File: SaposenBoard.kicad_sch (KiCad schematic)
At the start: 66 parts, among them IC1 BSO220, IC2 BSO220, IC3 BSO220, IC4 BSO220, J1 ADC4ch, J2 Extra2ch+LED, J3 Encoder1, J4 Encoder2, J5 I2C, J6 Battery, J7 Motor1, J8 Motor2, Q2 IRLML6344, SW1 BatterySW, SW2 SW_Push, SW3 SW_Push, U1 A4955GLPTR-T, U2 A4955GLPTR-T, U3 MPU-6500, U4 NUCLEO-F303K8

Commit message: [add]配線できた
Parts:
- removed J4: Encoder2, Connector_Molex:Molex_Micro-Latch_53253-0470_1x04_P2.00mm_Vertical, symbol Connector_Generic:Conn_01x04
- removed R23, R24, R25: 10k, Resistor_SMD:R_0603_1608Metric, symbol Device:R
- removed R5: 1k, Resistor_SMD:R_0603_1608Metric, symbol Device:R
- added J5: Encoder2, Connector_Molex:Molex_Micro-Latch_53253-0470_1x04_P2.00mm_Vertical, symbol Connector_Generic:Conn_01x04
- added Q2, Q3, Q4, Q5: IRLML6344, Package_TO_SOT_SMD:SOT-23, symbol Transistor_FET:BSS138
- added R15, R16, R17, R18, R19, R20, R21: 10k, Resistor_SMD:R_0603_1608Metric, symbol Device:R
- FB1: value FerriteBead_Small -> FerriteBead
- J3: renamed from J5; footprint Connector_Molex:Molex_Micro-Latch_53253-0470_1x04_P2.00mm_Vertical -> Connector_PinHeader_2.54mm:PinHeader_1x04_P2.54mm_Vertical
- renumbered C2 to C1, C15 to C10, C6 to C11, C16 to C12, C17 to C13, C1 to C14, C9 to C15, C10 to C16, C11 to C17, C8 to C2, C12 to C3, C3 to C4, C4 to C5, C7 to C6, C13 to C7, C14 to C8, C5 to C9, D2 to D1, D1 to D2, J3 to J4, J7 to J6, J8 to J7, J6 to J8, Q2 to Q1, R20 to R11, R3 to R12, R8 to R13, R7 to R14, R6 to R2, R16 to R23, R2 to R24, R4 to R25, R11 to R26, R12 to R27, R13 to R28, R21 to R3, R14 to R4, R17 to R5, R15 to R6, R18 to R7, R9 to R8, R19 to R9, SW2 to SW1, SW3 to SW2, SW1 to SW3
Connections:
- net +3V3: now also J3.2 (Pin_2), R22.2, Q2.1 (G), Q3.1 (G), Q4.1 (G), Q5.1 (G), R19.2, R20.2, R21.2; no longer J3.4 (Pin_4)
- net +5V: now also J5.4 (Pin_4), R15.2, R16.2, R17.2, R18.2; no longer R22.2
- net +BATT: now also FB1.2; no longer FB1.1
- net ENC1_1: now also Q3.2 (S), R19.1; no longer J4.3 (Pin_3)
- net ENC1_2: now also Q2.2 (S), R21.1; no longer J4.2 (Pin_2), R22.1
- net ENC2_1: now also Q5.2 (S), R20.1
- net ENC2_2: now also R22.1, Q4.2 (S)
- net Extra1: now also U4.3_14 (PB_5); no longer U4.3_15 (PB_4)
- net Extra2: now also U4.3_15 (PB_4); no longer U4.3_14 (PB_5)
- net GND: now also J5.1 (Pin_1)
- net SDA: now also J3.4 (Pin_4); no longer J3.2 (Pin_2)
- net at U4.4_1 (VIN): now also FB1.1; no longer FB1.2
- net VBAT: no longer names the net of D2.1 (K), R24.2, R25.1, U4.4_9 (PA_4)
- new net: J4.2 (Pin_2), Q3.3 (D), R17.1
- new net: J5.2 (Pin_2), Q5.3 (D), R18.1
- new net: J5.3 (Pin_3), Q4.3 (D), R16.1
- new net: J4.3 (Pin_3), Q2.3 (D), R15.1
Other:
- moved on the sheet: BZ1, C1, C14, C4, D1, D2, FB1, J3, J4, J8, Q1, R1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

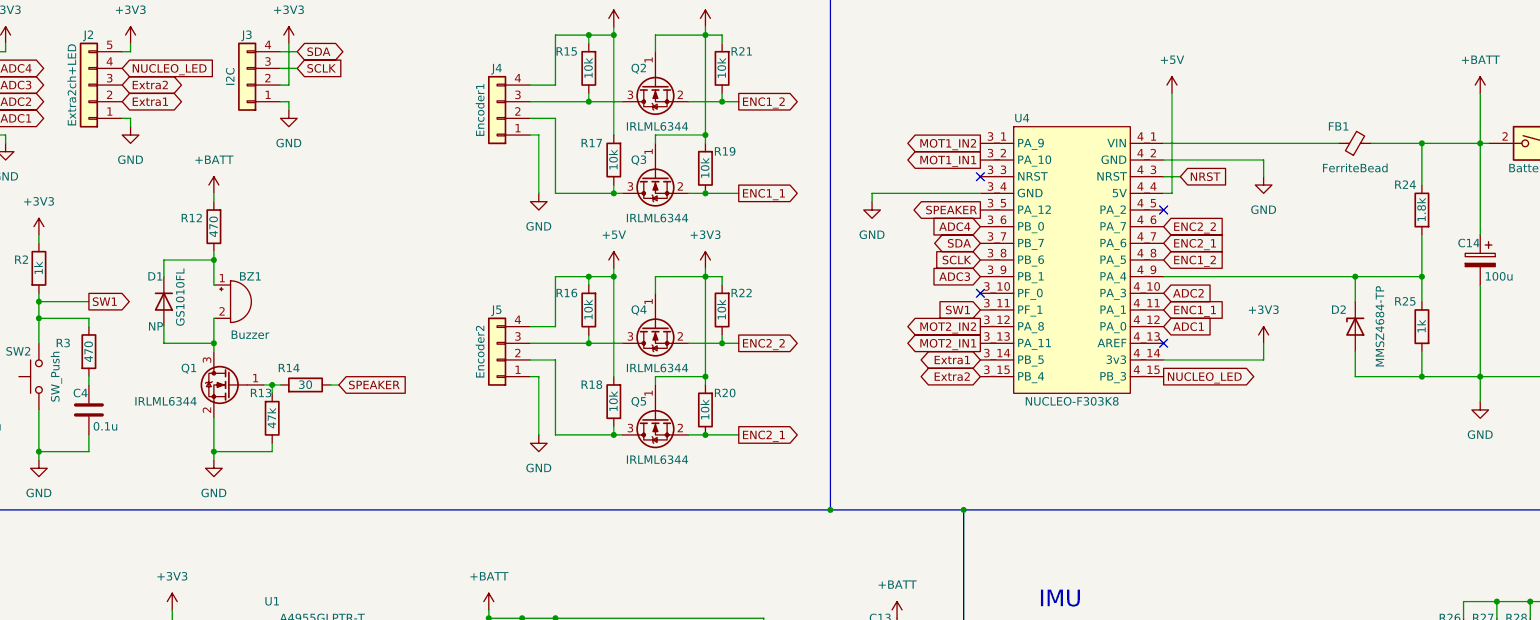
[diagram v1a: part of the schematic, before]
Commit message: [fix]部品を変更
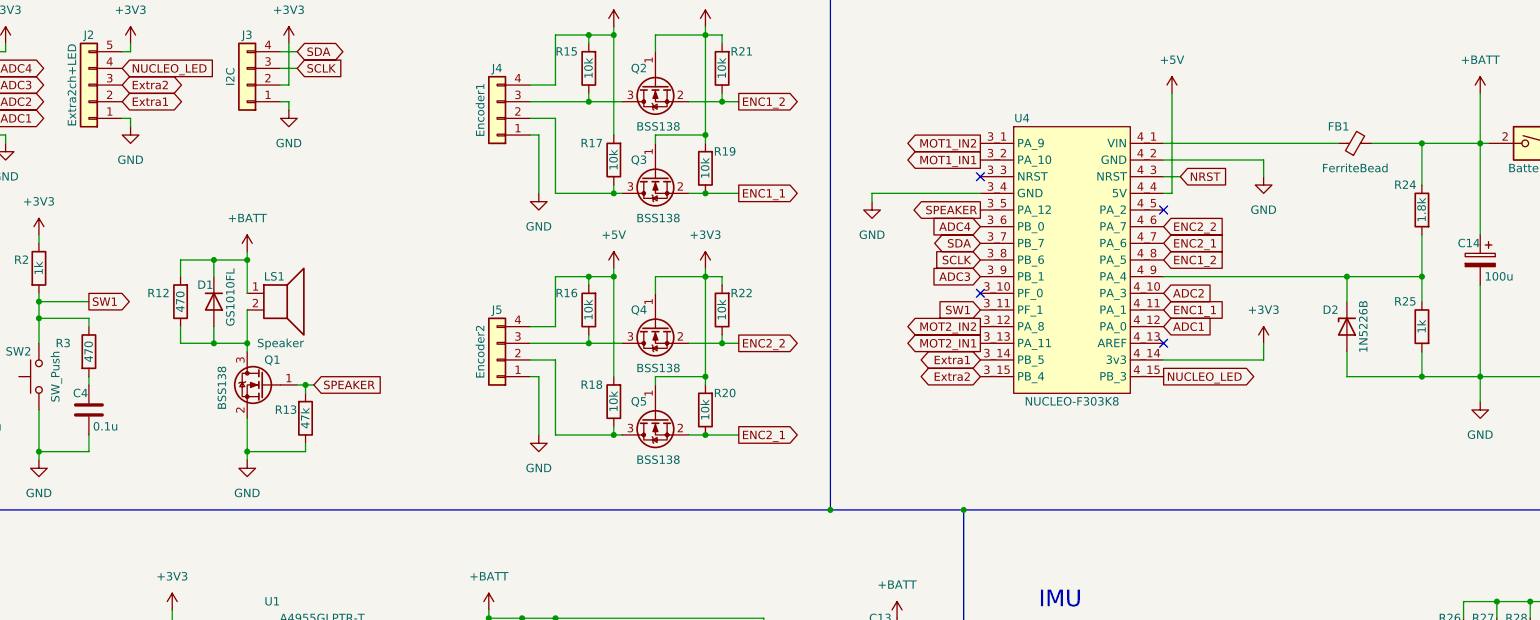
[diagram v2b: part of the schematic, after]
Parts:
- removed R14: 30, Resistor_SMD:R_0603_1608Metric, symbol Device:R
- D2: value MMSZ4684-TP -> 1N5226B; footprint Diode_SMD:D_SOD-123 -> Diode_THT:D_DO-35_SOD27_P2.54mm_Vertical_KathodeUp
- LS1: renamed from BZ1; value Buzzer -> Speaker; symbol Device:Buzzer -> Device:Speaker
- Q1, Q2, Q3, Q4, Q5: value IRLML6344 -> BSS138
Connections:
- net +BATT: now also D1.1 (K), LS1.1
- net SPEAKER: now also Q1.1 (G), R13.2
- net at D1.2 (A), LS1.2, Q1.3 (D): now also R12.1
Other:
- moved on the sheet: D1, D2, R13

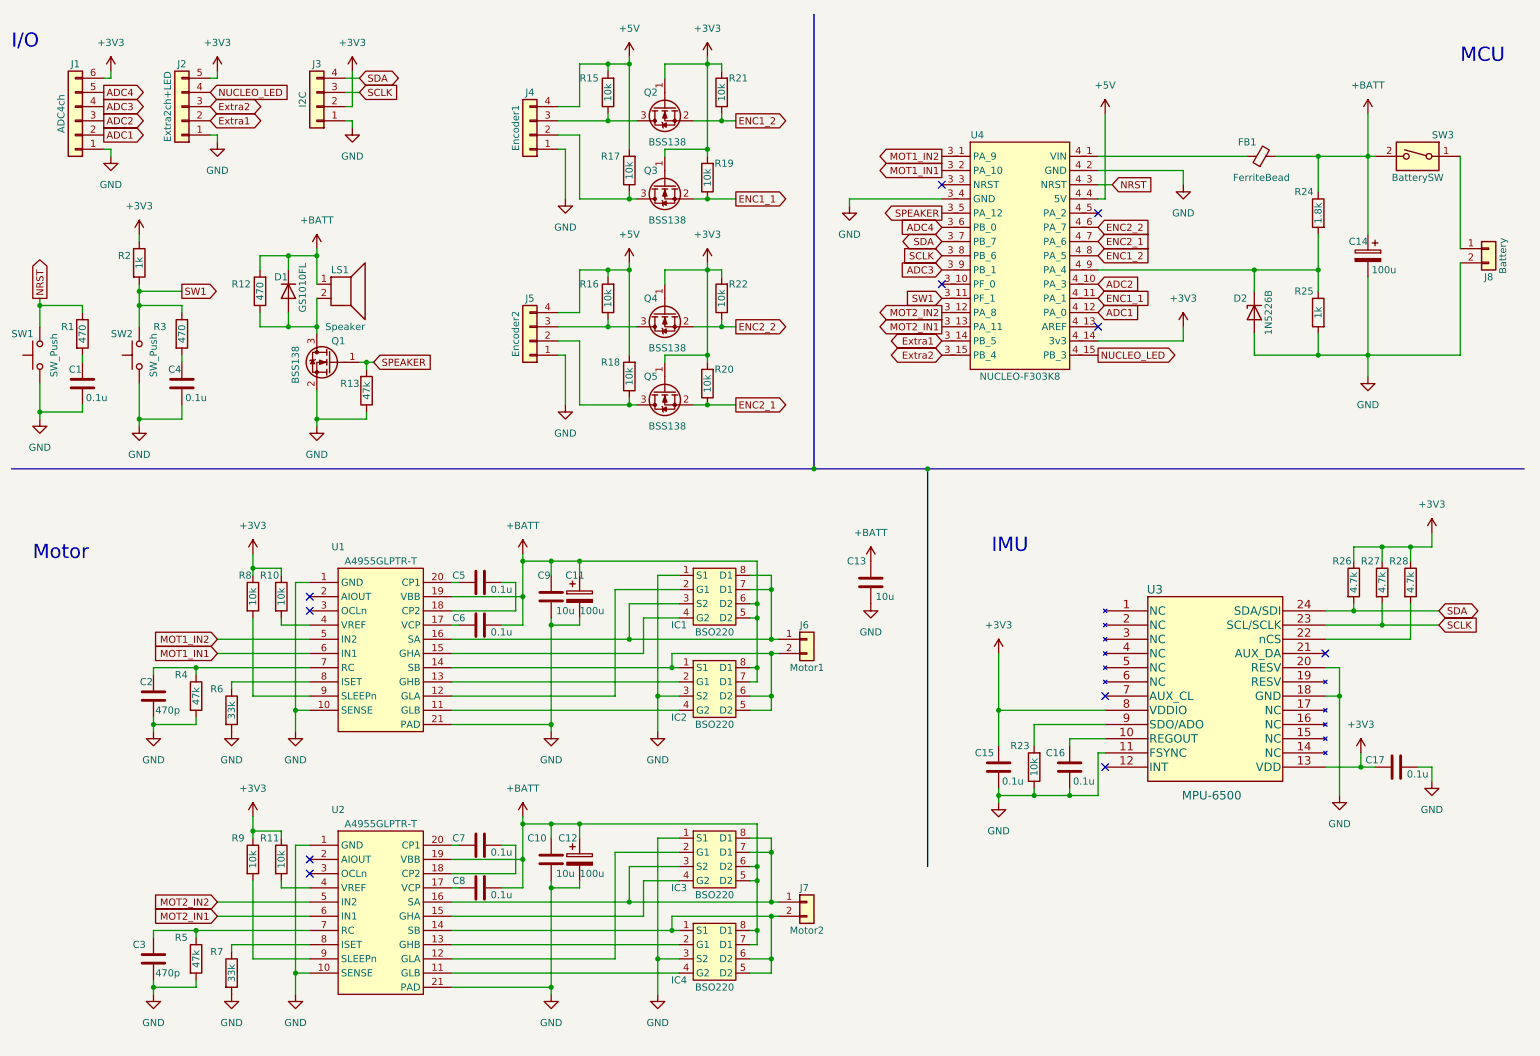
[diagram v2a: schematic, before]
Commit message: [add]ロゴ変更
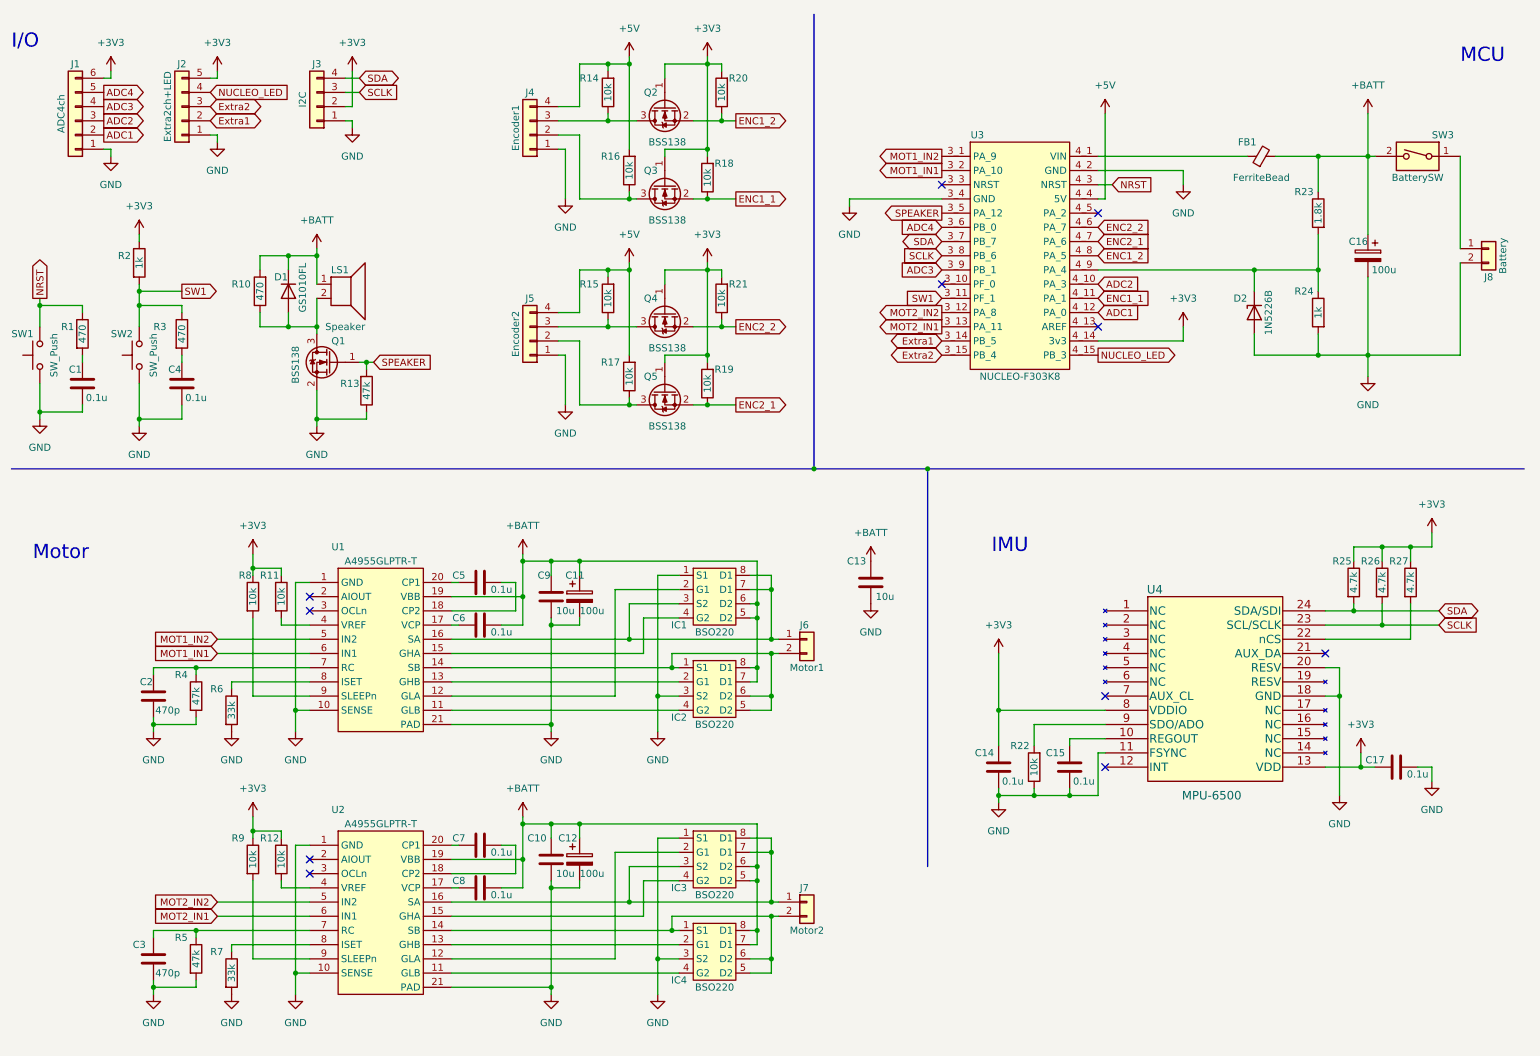
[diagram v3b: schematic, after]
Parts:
- renumbered C15 to C14, C16 to C15, C14 to C16, R12 to R10, R10 to R11, R11 to R12, R15 to R14, R16 to R15, R17 to R16, R18 to R17, R19 to R18, R20 to R19, R21 to R20, R22 to R21, R23 to R22, R24 to R23, R25 to R24, R26 to R25, R27 to R26, R28 to R27, U4 to U3, U3 to U4

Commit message: [update]モータードライバの入力を変換
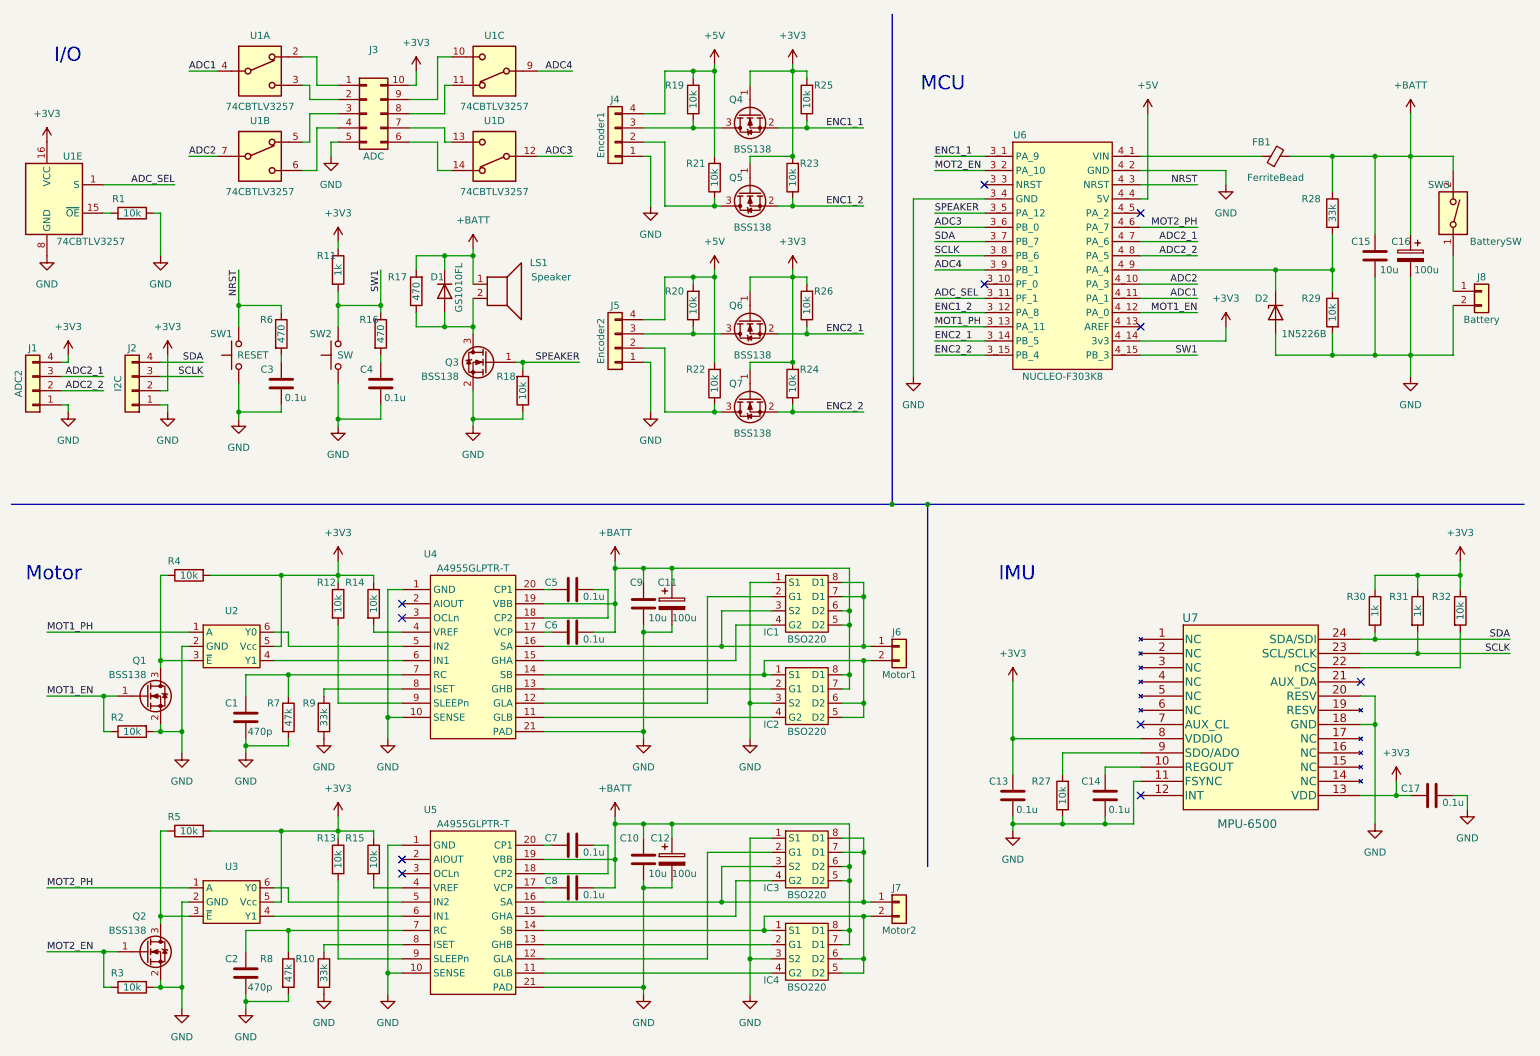
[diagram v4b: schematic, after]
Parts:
- removed C13: 10u, Capacitor_SMD:C_0805_2012Metric, symbol Device:C
- removed C3: 470p, Capacitor_SMD:C_0603_1608Metric, symbol Device:C
- removed J1: ADC4ch, Connector_Molex:Molex_Micro-Latch_53253-0670_1x06_P2.00mm_Vertical, symbol Connector_Generic:Conn_01x06
- removed J2: Extra2ch+LED, Connector_Molex:Molex_Micro-Latch_53253-0570_1x05_P2.00mm_Vertical, symbol Connector_Generic:Conn_01x05
- removed J3: I2C, Connector_PinHeader_2.54mm:PinHeader_1x04_P2.54mm_Vertical, symbol Connector_Generic:Conn_01x04
- removed R7: 33k, Resistor_SMD:R_0603_1608Metric, symbol Device:R
- added C15: 10u, Capacitor_SMD:C_0805_2012Metric, symbol Device:C
- added C2: 470p, Capacitor_SMD:C_0603_1608Metric, symbol Device:C
- added J1: ADC2, Connector_PinHeader_2.54mm:PinHeader_1x04_P2.54mm_Vertical, symbol Connector_Generic:Conn_01x04
- added J2: I2C, Connector_PinHeader_2.54mm:PinHeader_1x04_P2.54mm_Vertical, symbol Connector_Generic:Conn_01x04
- added J3: ADC, symbol Connector_Generic:Conn_02x05_Counter_Clockwise
- added Q1, Q2: BSS138, Package_TO_SOT_SMD:SOT-23, symbol Transistor_FET:BSS138
- added R1, R2, R3, R4: 10k, Resistor_SMD:R_0603_1608Metric, symbol Device:R
- added R10: 33k, Resistor_SMD:R_0603_1608Metric, symbol Device:R
- added R8: 47k, Resistor_SMD:R_0603_1608Metric, symbol Device:R
- added U1: 74CBTLV3257, symbol 74xx:74CBTLV3257
- added U2, U3: ~, symbol Symbols:NC7SZ19
- R18: renamed from R13; value 47k -> 10k
- R28: renamed from R23; value 1.8k -> 33k
- R29: renamed from R24; value 1k -> 10k
- R30: renamed from R25; value 4.7k -> 1k
- R31: renamed from R26; value 4.7k -> 1k
- R32: renamed from R27; value 4.7k -> 10k
- R5: value 47k -> 10k
- SW1: value SW_Push -> RESET
- SW2: value SW_Push -> SW
- renumbered C2 to C1, C14 to C13, C15 to C14, C1 to C3, Q1 to Q3, Q2 to Q4, Q3 to Q5, Q4 to Q6, Q5 to Q7, R2 to R11, R8 to R12, R9 to R13, R11 to R14, R12 to R15, R3 to R16, R10 to R17, R14 to R19, R15 to R20, R16 to R21, R17 to R22, R18 to R23, R19 to R24, R20 to R25, R21 to R26, R22 to R27, R1 to R6, R4 to R7, R6 to R9, U1 to U4, U2 to U5, U3 to U6, U4 to U7
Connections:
- net Extra1 is gone; now on net ENC2_1: U6.3_14 (PB_5)
- net Extra2 is gone; now on net ENC2_2: U6.3_15 (PB_4)
- net NUCLEO_LED is gone; now on net SW1: U6.4_15 (PB_3)
- net +3V3: now also R5.2, J1.4 (Pin_4), J2.2 (Pin_2), J3.10 (Pin_10), R4.2, U1.16 (VCC), U2.5 (Vcc), U3.5 (Vcc)
- net +BATT: now also C15.2
- net ADC1: now also U6.4_11 (PA_1), U1.4; no longer U6.4_12 (PA_0)
- net ADC2: now also U1.7
- net ADC3: now also U6.3_6 (PB_0), U1.12; no longer U6.3_9 (PB_1)
- net ADC4: now also U6.3_9 (PB_1), U1.9; no longer U6.3_6 (PB_0)
- net ENC1_1: now also Q4.2 (S), R25.1, U6.3_1 (PA_9); no longer Q5.2 (S), R23.1, U6.4_11 (PA_1)
- net ENC1_2: now also Q5.2 (S), R23.1, U6.3_12 (PA_8); no longer Q4.2 (S), R25.1, U6.4_8 (PA_5)
- net ENC2_1: now also Q6.2 (S), R26.1; no longer Q7.2 (S), R24.1, U6.4_7 (PA_6)
- net ENC2_2: now also Q7.2 (S), R24.1; no longer Q6.2 (S), R26.1, U6.4_6 (PA_7)
- net GND: now also C15.1, C2.2, J1.1 (Pin_1), J2.1 (Pin_1), J3.5 (Pin_5), Q1.2 (S), Q2.2 (S), R1.1, R10.2, R2.2, R3.2, R8.2, U1.8 (GND), U2.2 (GND), U3.2 (GND); no longer R5.2
- net SCLK: now also J2.3 (Pin_3)
- net SDA: now also J2.4 (Pin_4)
- net SW1: no longer U6.3_11 (PF_1)
- net at U5.7 (RC): now also C2.1, R8.1; no longer R5.1
- net at U5.8 (ISET): now also R10.1
- net MOT1_IN1: no longer names the net of U4.6 (IN1)
- net MOT1_IN1: now also U2.4 (Y1); no longer U6.3_2 (PA_10)
- net MOT1_IN2: no longer names the net of U4.5 (IN2)
- net MOT1_IN2: now also U2.6 (Y0); no longer U6.3_1 (PA_9)
- net MOT2_IN1: no longer names the net of U5.6 (IN1)
- net MOT2_IN1: now also U3.4 (Y1); no longer U6.3_13 (PA_11)
- net MOT2_IN2: no longer names the net of U5.5 (IN2)
- net MOT2_IN2: now also U3.6 (Y0); no longer U6.3_12 (PA_8)
- new net: J3.1 (Pin_1), U1.2
- new net: J3.2 (Pin_2), U1.3
- new net: J3.7 (Pin_7), U1.13
- new net: J3.6 (Pin_6), U1.14
- new net: Q1.3 (D), R4.1, U2.3 (~{E})
- new net: J3.9 (Pin_9), U1.10
- new net: J3.8 (Pin_8), U1.11
- new net: J3.3 (Pin_3), U1.5
- new net: J3.4 (Pin_4), U1.6
- new net: R1.2, U1.15 (~{OE})
- new net: Q2.3 (D), R5.1, U3.3 (~{E})
- new net ADC2_1: J1.3 (Pin_3), U6.4_7 (PA_6)
- new net ADC2_2: J1.2 (Pin_2), U6.4_8 (PA_5)
- new net ADC_SEL: U1.1 (S), U6.3_11 (PF_1)
- new net MOT1_EN: Q1.1 (G), R2.1, U6.4_12 (PA_0)
- new net MOT1_PH: U2.1 (A), U6.3_13 (PA_11)
- new net MOT2_EN: Q2.1 (G), R3.1, U6.3_2 (PA_10)
- new net MOT2_PH: U3.1 (A), U6.4_6 (PA_7)
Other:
- moved on the sheet: C1, C10, C11, C12, C13, C14, C16, C17, C3, C4, C5, C6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
